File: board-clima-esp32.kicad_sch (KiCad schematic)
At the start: 54 parts, among them IC1 ESP32-S3-WROOM-1-N4, J1 Conn_01x06_Pin, J2 Screw_Terminal_01x03, J3 Conn_01x04_Pin, J5 Conn_01x05_Pin, J6 USB_C_Receptacle, Q1 AO3400A, Q2 AO3401A, Q3 AO3400A, SW1 RESET, SW2 BOOT, U1 AMS1117-3.3, U3 PC817, U4 PC817

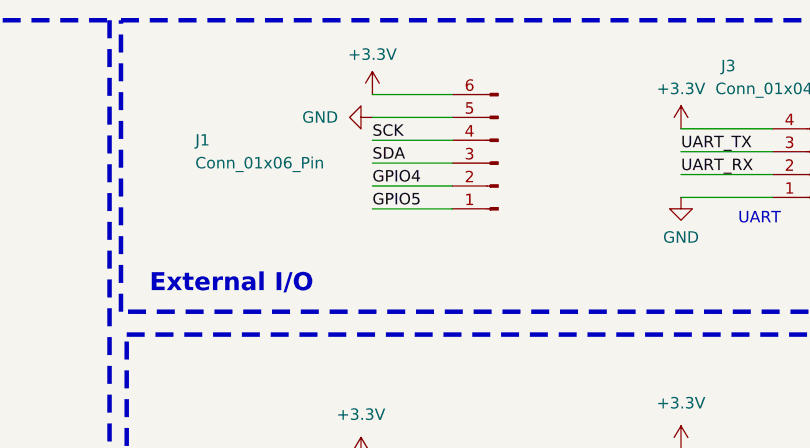
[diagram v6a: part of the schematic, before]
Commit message: New J1 connector location
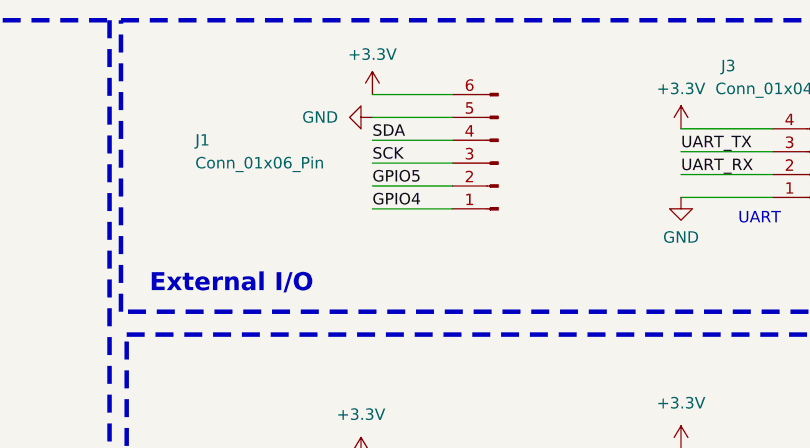
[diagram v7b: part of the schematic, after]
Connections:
- net GPIO4: now also J1.1 (Pin_1); no longer J1.2 (Pin_2)
- net GPIO5: now also J1.2 (Pin_2); no longer J1.1 (Pin_1)
- net SCK: now also J1.3 (Pin_3); no longer J1.4 (Pin_4)
- net SDA: now also J1.4 (Pin_4); no longer J1.3 (Pin_3)
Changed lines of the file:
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@@
     (effects (font (size 1.27 1.27)) (justify left bottom))
   )
-  (label "GPIO4" (at 300.99 33.02 0) (fields_autoplaced)
+  (label "GPIO5" (at 300.99 33.02 0) (fields_autoplaced)
     (effects (font (size 1.27 1.27)) (justify left bottom))
   )
@@
     (effects (font (size 1.27 1.27)) (justify left bottom))
   )
-  (label "SCK" (at 300.99 27.94 0) (fields_autoplaced)
+  (label "SDA" (at 300.99 27.94 0) (fields_autoplaced)
     (effects (font (size 1.27 1.27)) (justify left bottom))
   )
@@
     (effects (font (size 1.27 1.27)) (justify left bottom))
   )
-  (label "SDA" (at 300.99 30.48 0) (fields_autoplaced)
+  (label "SCK" (at 300.99 30.48 0) (fields_autoplaced)
     (effects (font (size 1.27 1.27)) (justify left bottom))
   )
@@
     (effects (font (size 1.27 1.27)) (justify left bottom))
   )
-  (label "GPIO5" (at 300.99 35.56 0) (fields_autoplaced)
+  (label "GPIO4" (at 300.99 35.56 0) (fields_autoplaced)
     (effects (font (size 1.27 1.27)) (justify left bottom))
   )
@@
       (effects (font (size 1.27 1.27)) hide)
     )
+    (pin "1")
+    (pin "11")
+    (pin "13")
+    (pin "15")
+    (pin "16")
+    (pin "2")
+    (pin "4")
+    (pin "6")
+    (pin "8")
     (pin "9")
-    (pin "11")
-    (pin "1")
-    (pin "6")
-    (pin "13")
-    (pin "2")
-    (pin "4")
-    (pin "16")
-    (pin "15")
-    (pin "8")
     (instances
       (project "board-clima-esp32"
@@
       (effects (font (size 1.27 1.27)) hide)
     )
-    (pin "2")
-    (pin "1")
+    (pin "1")
+    (pin "2")
     (instances
       (project "board-clima-esp32"
@@
       (effects (font (size 1.27 1.27)) hide)
     )
-    (pin "2")
-    (pin "1")
+    (pin "1")
+    (pin "2")
     (instances
       (project "board-clima-esp32"
@@
       (effects (font (size 1.27 1.27)) hide)
     )
-    (pin "2")
-    (pin "1")
+    (pin "1")
+    (pin "2")
     (instances
       (project "board-clima-esp32"
@@
     (pin "1")
     (pin "2")
+    (pin "3")
     (pin "4")
-    (pin "3")
     (instances
       (project "board-clima-esp32"
@@
       (effects (font (size 1.27 1.27)) hide)
     )
-    (pin "2")
-    (pin "1")
+    (pin "1")
+    (pin "2")
     (instances
       (project "board-clima-esp32"
@@
       (effects (font (size 1.27 1.27)) hide)
     )
-    (pin "2")
-    (pin "1")
+    (pin "1")
+    (pin "2")
     (instances
       (project "board-clima-esp32"
@@
       (effects (font (size 1.27 1.27)) (justify left) hide)
     )
-    (pin "2")
-    (pin "1")
+    (pin "1")
+    (pin "2")
     (pin "3")
     (instances
@@
       (effects (font (size 1.27 1.27)) hide)
     )
-    (pin "2")
-    (pin "1")
+    (pin "1")
+    (pin "2")
     (instances
       (project "board-clima-esp32"
@@
       (effects (font (size 1.27 1.27)) (justify left) hide)
     )
+    (pin "1")
+    (pin "2")
     (pin "3")
-    (pin "2")
-    (pin "1")
     (instances
       (project "board-clima-esp32"
@@
       (effects (font (size 1.27 1.27)) hide)
     )
-    (pin "2")
-    (pin "1")
+    (pin "1")
+    (pin "2")
     (instances
       (project "board-clima-esp32"
@@
     (pin "1")
     (pin "2")
+    (pin "3")
     (pin "4")
-    (pin "3")
     (instances
       (project "board-clima-esp32"
@@
       (effects (font (size 1.27 1.27)) hide)
     )
-    (pin "2")
-    (pin "1")
+    (pin "1")
+    (pin "2")
     (instances
       (project "board-clima-esp32"
@@
       (effects (font (size 1.27 1.27)) (justify left) hide)
     )
-    (pin "2")
-    (pin "1")
+    (pin "1")
+    (pin "2")
     (pin "3")
     (instances

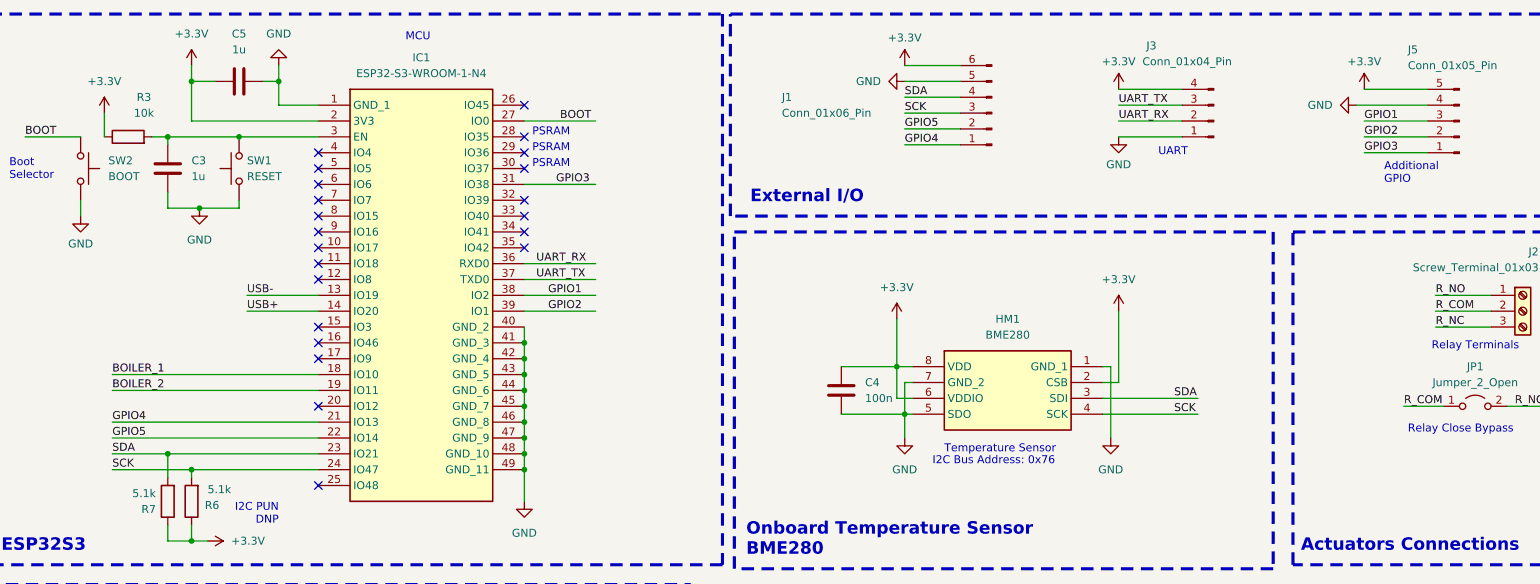
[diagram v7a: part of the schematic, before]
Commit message: Cleanup pcb layout for easier routing
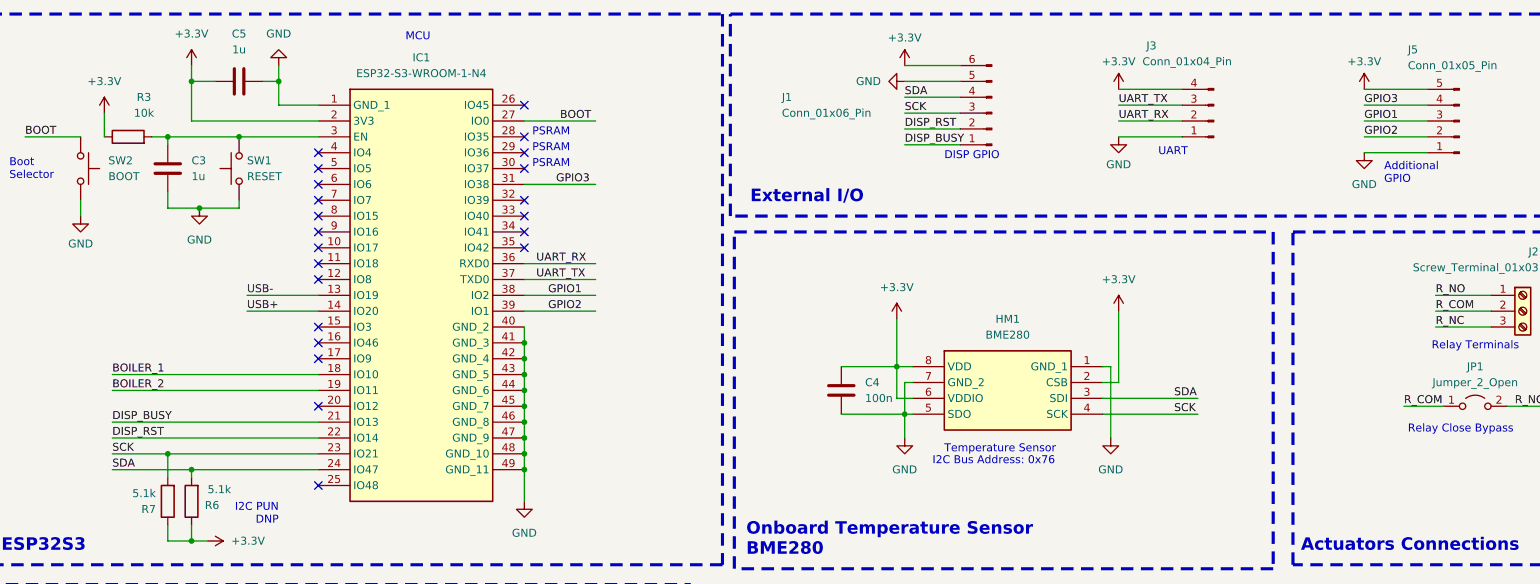
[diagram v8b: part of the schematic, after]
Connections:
- net GND: now also J5.1 (Pin_1); no longer J5.4 (Pin_4)
- net GPIO3: now also J5.4 (Pin_4); no longer J5.1 (Pin_1)
- net SCK: now also IC1.23 (IO21), R7.2; no longer IC1.24 (IO47), R6.2
- net SDA: now also IC1.24 (IO47), R6.2; no longer IC1.23 (IO21), R7.2
- net GPIO4 renamed DISP_BUSY
- net GPIO5 renamed DISP_RST
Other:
- note added: "DISP GPIO"
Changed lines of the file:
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@@
-    (stroke (width 0) (type default))
-  )
-  (wire (pts (xy 373.38 29.21) (xy 384.81 29.21))
     (stroke (width 0) (type default))
   )
@@
   )
   (wire (pts (xy 186.69 99.06) (xy 186.69 96.52))
+    (stroke (width 0) (type default))
+  )
+  (wire (pts (xy 374.65 29.21) (xy 384.81 29.21))
     (stroke (width 0) (type default))
   )
@@
     (effects (font (size 2 2) (thickness 0.4) bold) (justify left bottom))
   )
+  (text "DISP GPIO" (at 307.34 38.1 0)
+    (effects (font (size 1.27 1.27)) (justify left bottom))
+  )
   (text "USB In" (at 34.925 89.535 0)
     (effects (font (size 1.27 1.27)) (justify left bottom))
@@
     (effects (font (size 1.27 1.27)) (justify left bottom))
   )
-  (label "GPIO5" (at 300.99 33.02 0) (fields_autoplaced)
+  (label "DISP_RST" (at 300.99 33.02 0) (fields_autoplaced)
     (effects (font (size 1.27 1.27)) (justify left bottom))
   )
@@
     (effects (font (size 1.27 1.27)) (justify left bottom))
   )
-  (label "SDA" (at 173.99 85.09 0) (fields_autoplaced)
-    (effects (font (size 1.27 1.27)) (justify left bottom))
-  )
-  (label "GPIO4" (at 173.99 80.01 0) (fields_autoplaced)
+  (label "SCK" (at 173.99 85.09 0) (fields_autoplaced)
+    (effects (font (size 1.27 1.27)) (justify left bottom))
+  )
+  (label "DISP_BUSY" (at 173.99 80.01 0) (fields_autoplaced)
     (effects (font (size 1.27 1.27)) (justify left bottom))
   )
@@
     (effects (font (size 1.27 1.27)) (justify left bottom))
   )
-  (label "GPIO5" (at 173.99 82.55 0) (fields_autoplaced)
+  (label "DISP_RST" (at 173.99 82.55 0) (fields_autoplaced)
     (effects (font (size 1.27 1.27)) (justify left bottom))
   )
@@
     (effects (font (size 1.27 1.27)) (justify left bottom))
   )
-  (label "GPIO3" (at 374.65 36.83 0) (fields_autoplaced)
-    (effects (font (size 1.27 1.27)) (justify left bottom))
-  )
   (label "GPIO3" (at 245.11 41.91 0) (fields_autoplaced)
     (effects (font (size 1.27 1.27)) (justify left bottom))
@@
     (effects (font (size 1.27 1.27)) (justify left bottom))
   )
-  (label "SCK" (at 173.99 87.63 0) (fields_autoplaced)
+  (label "SDA" (at 173.99 87.63 0) (fields_autoplaced)
     (effects (font (size 1.27 1.27)) (justify left bottom))
   )
@@
     (effects (font (size 1.27 1.27)) (justify left bottom))
   )
-  (label "GPIO4" (at 300.99 35.56 0) (fields_autoplaced)
+  (label "DISP_BUSY" (at 300.99 35.56 0) (fields_autoplaced)
     (effects (font (size 1.27 1.27)) (justify left bottom))
   )
@@
     (effects (font (size 1.27 1.27)) (justify left bottom))
   )
+  (label "GPIO3" (at 374.65 29.21 0) (fields_autoplaced)
+    (effects (font (size 1.27 1.27)) (justify left bottom))
+  )
   (label "R_NO" (at 175.26 130.81 0) (fields_autoplaced)
     (effects (font (size 1.27 1.27)) (justify left bottom))
@@
     (effects (font (size 1.27 1.27)) (justify left bottom))
   )
-  (symbol (lib_id "power:GND") (at 373.38 29.21 270) (unit 1)
+  (symbol (lib_id "power:GND") (at 374.65 36.83 0) (unit 1)
     (in_bom yes) (on_board yes) (dnp no) (fields_autoplaced)
-    (property "Reference" "#PWR034" (at 367.03 29.21 0)
+    (property "Reference" "#PWR034" (at 374.65 43.18 0)
       (effects (font (size 1.27 1.27)) hide)
     )
-    (property "Value" "GND" (at 369.57 29.21 90)
-      (effects (font (size 1.27 1.27)) (justify right))
+    (property "Value" "GND" (at 374.65 41.91 0)
+      (effects (font (size 1.27 1.27)))
     )
-    (property "Footprint" "" (at 373.38 29.21 0)
+    (property "Footprint" "" (at 374.65 36.83 0)
       (effects (font (size 1.27 1.27)) hide)
     )
-    (property "Datasheet" "" (at 373.38 29.21 0)
+    (property "Datasheet" "" (at 374.65 36.83 0)
       (effects (font (size 1.27 1.27)) hide)
     )
